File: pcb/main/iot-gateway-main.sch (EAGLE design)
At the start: 261 parts, among them CON1 6P-SH-TOP, CON2 3P-SH-TOP, CON3 2P-PH-TOP, CON4 6P-SH-TOP, CON5 3P-SH-TOP, CON6 5P-SH-TOP, CON7 2P-PH-TOP, Q1 AO3400, Q2 AO3400, Q3 AO3400, Q4 FS8205, T1 BC817, U1 SST26VF064B, U10 SIM800C, U11 SI7021, U12 SI7210, U13 BMP280, U14 CCS811, U15 TMG39933, U16 ER-TFT035-6-BOT, U17 74LVC1G11, U18 74LVC1G17, U19 LTC4313-1, U2 EFM32GG11B820F2048GQ100, U20 LT8636, U21 MIC23159, U22 74LVC1G04, U23 LTC2942, U24 LTC4040, U25 FS312F-G, U3 SST26VF016B, U4 ESP8266EX, U5 RFM69HW, U6 74LVC1G332, U7 74LVC1G332, U8 74LVC1G32, U9 74LVC1G08, X1 24 MHz, X2 32.768 kHz, X3 26 MHz

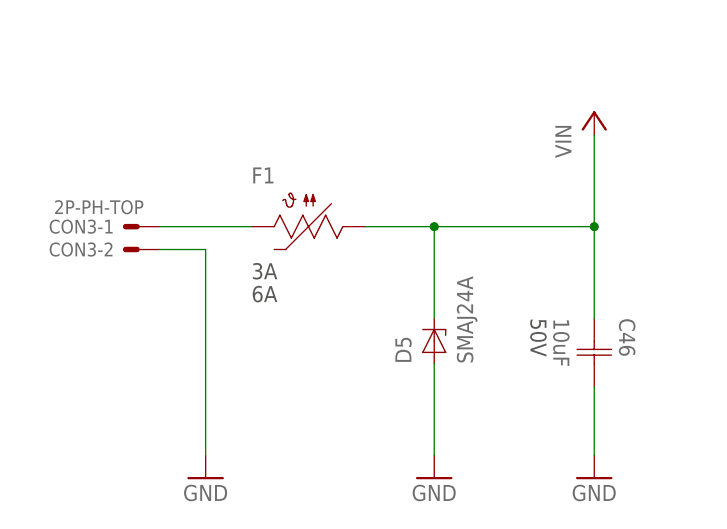
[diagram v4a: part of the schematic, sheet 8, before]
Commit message: Fix ADC precision loss by right shift instead of dividing (already fixed before but came back?)
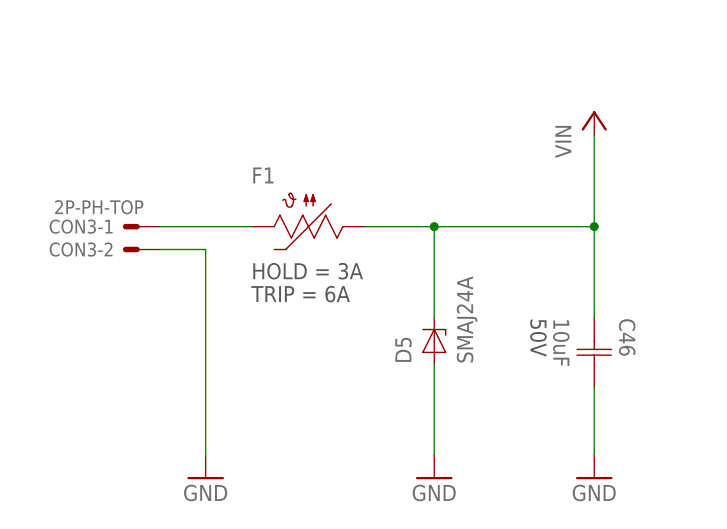
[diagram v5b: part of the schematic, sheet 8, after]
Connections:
- net N$37 renamed 5V0_GATE
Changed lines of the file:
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@@
 <instance part="F1" gate="G$1" x="48.26" y="50.8" smashed="yes">
 <attribute name="OCLCSC" x="48.26" y="50.8" size="1.778" layer="96" display="off"/>
-<attribute name="HOLD" x="48.26" y="46.736" size="1.778" layer="97" align="top-left"/>
-<attribute name="TRIP" x="48.26" y="44.196" size="1.778" layer="97" align="top-left"/>
+<attribute name="HOLD" x="48.26" y="46.736" size="1.778" layer="97" align="top-left" display="both"/>
+<attribute name="TRIP" x="48.26" y="44.196" size="1.778" layer="97" align="top-left" display="both"/>
 <attribute name="NAME" x="48.26" y="55.6006" size="1.778" layer="95" ratio="10" rot="SR0"/>
 </instance>
@@
 </segment>
 </net>
-<net name="N$37" class="0">
+<net name="5V0_GATE" class="0">
 <segment>
 <pinref part="U24" gate="G$1" pin="IGATE"/>

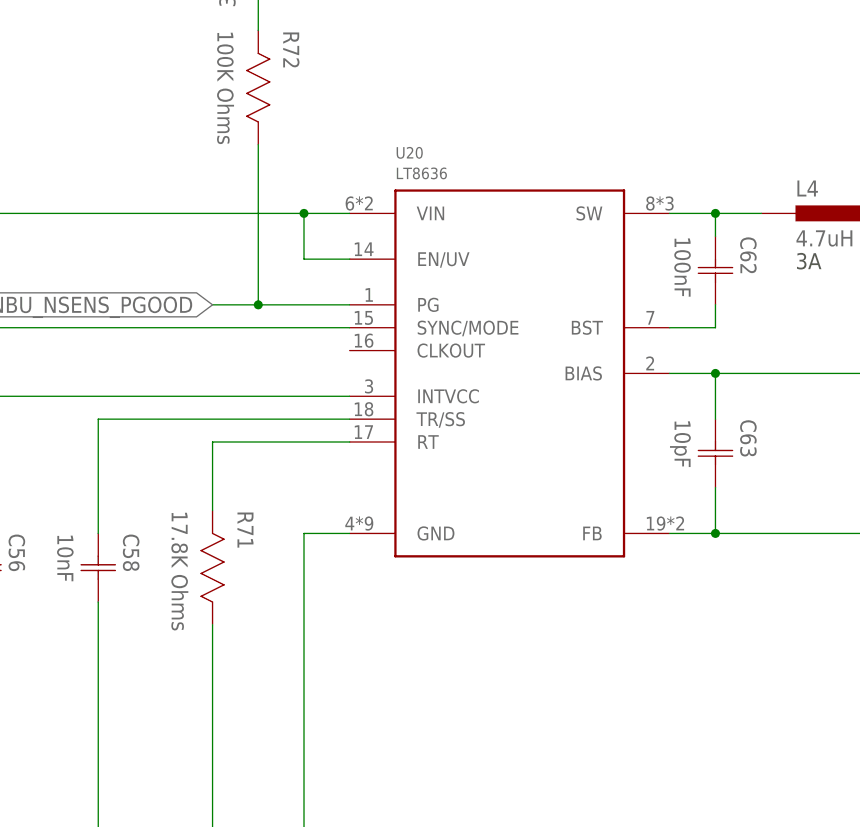
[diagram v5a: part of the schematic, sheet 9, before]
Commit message: Change 5V_NBU regulator to LT8640S
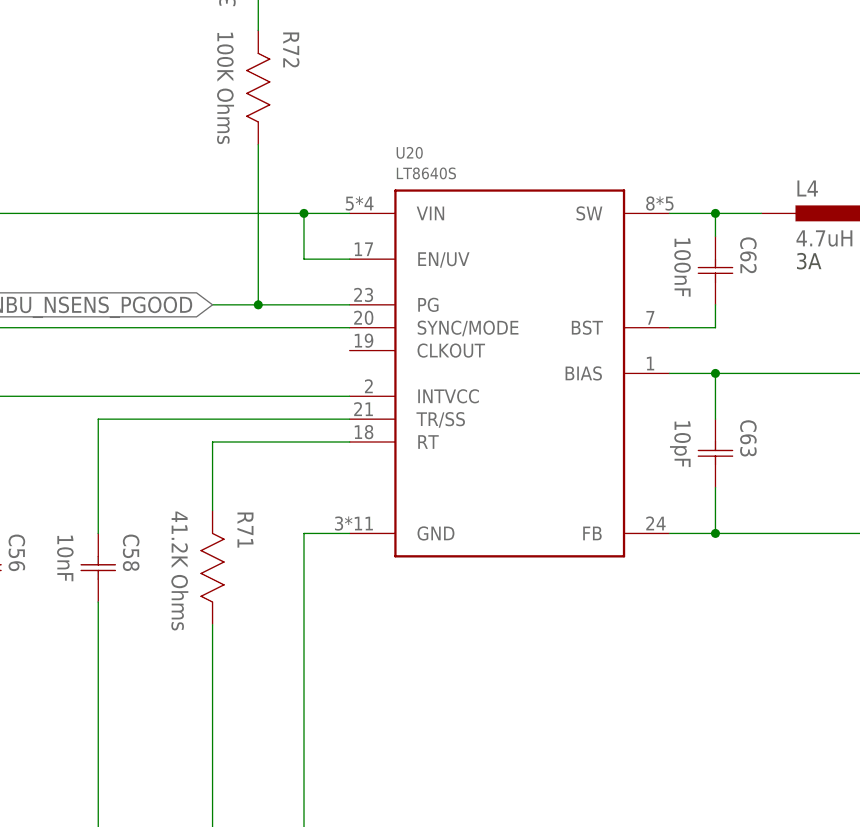
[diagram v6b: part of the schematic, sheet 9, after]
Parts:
- R71: value 17.8K Ohms -> 41.2K Ohms
- U20: value LT8636 -> LT8640S; device Analog Devices:LT8636 -> Analog Devices:LT8640S
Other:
- note added: "Vbkpstart = ((R83/R84) + 1) * 1.19"
- note added: "f = 1 MHz DS. Eq. 3 & Table 1"
- note removed: "Vbkpstart = 1.19 / (R75/(R75+R76))"
- note removed: "f = 2 MHz DS. Eq. 3 & Table 1"
- moved on the sheet: U20
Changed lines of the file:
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@@
 <?xml version="1.0" encoding="utf-8"?>
 <!DOCTYPE eagle SYSTEM "eagle.dtd">
-<eagle version="9.5.1">
+<eagle version="9.5.2">
 <drawing>
 <settings>
@@
 <part name="C58" library="Capacitor" deviceset="CAPACITOR" device="-0603" value="10nF"/>
 <part name="C56" library="Capacitor" deviceset="CAPACITOR" device="-0603" value="1uF"/>
-<part name="R71" library="Resistor" deviceset="RESISTOR" device="-0603" value="17.8K Ohms"/>
+<part name="R71" library="Resistor" deviceset="RESISTOR" device="-0603" value="41.2K Ohms"/>
 <part name="L4" library="Inductor" deviceset="INDUCTOR" device="-6X6MM" value="4.7uH">
 <attribute name="CURRENT" value="3A"/>
@@
 <part name="5V02" library="Supply Symbol" deviceset="5V0" device=""/>
 <part name="GND89" library="Supply Symbol" deviceset="GND" device=""/>
-<part name="U20" library="Analog Devices" deviceset="LT8636" device=""/>
+<part name="U20" library="Analog Devices" deviceset="LT8640S" device=""/>
 <part name="C52" library="Capacitor" deviceset="CAPACITOR" device="-0603" value="1uF">
 <attribute name="VOLTAGE" value="50V"/>
@@
 <description>Power Management</description>
 <plain>
-<text x="121.92" y="269.24" size="1.4224" layer="98" rot="R90">f = 2 MHz
+<text x="121.92" y="269.24" size="1.4224" layer="98" rot="R90">f = 1 MHz
 DS. Eq. 3 &amp; Table 1</text>
 <text x="386.842" y="290.322" size="1.27" layer="98" rot="R180">VBAT = 4.1V
@@
 <text x="485.902" y="310.642" size="1.27" layer="98" rot="R180">Vout = ((R96/R97) + 1) * 0.8</text>
 <text x="214.122" y="305.562" size="1.27" layer="98" rot="R180">Vout = ((R78/R79) + 1) * 0.97</text>
-<text x="323.342" y="320.802" size="1.27" layer="98" rot="R180">Vbkpstart = 1.19 / (R75/(R75+R76))</text>
+<text x="320.802" y="320.802" size="1.27" layer="98" rot="R180">Vbkpstart = ((R83/R84) + 1) * 1.19</text>
 <text x="485.14" y="198.12" size="1.4224" layer="98">For LiPo use FS312F-G
 For Li-ion use DW01A-G</text>
